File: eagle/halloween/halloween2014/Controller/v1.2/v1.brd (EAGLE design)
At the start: 99.2 x 69.3 mm, 74 parts, among them CON1 SPI, J1 RJ12, J2 RJ12, J3 RJ12, J4 RJ12, J5 RJ12, Q1 BSP75, Q10 BSP75, Q11 BSP75, Q12 BSP75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

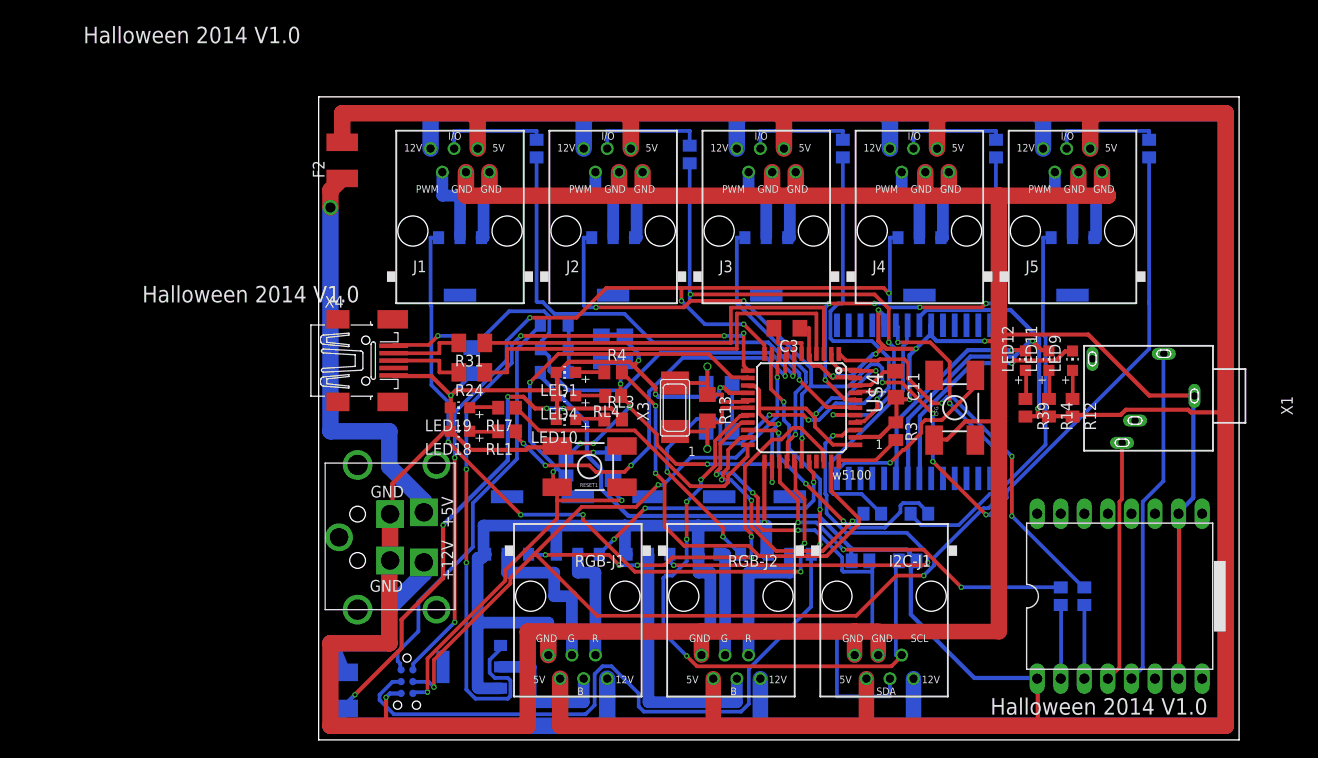
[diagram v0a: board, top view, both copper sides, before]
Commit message: Update halloween, corredt D8 - D10
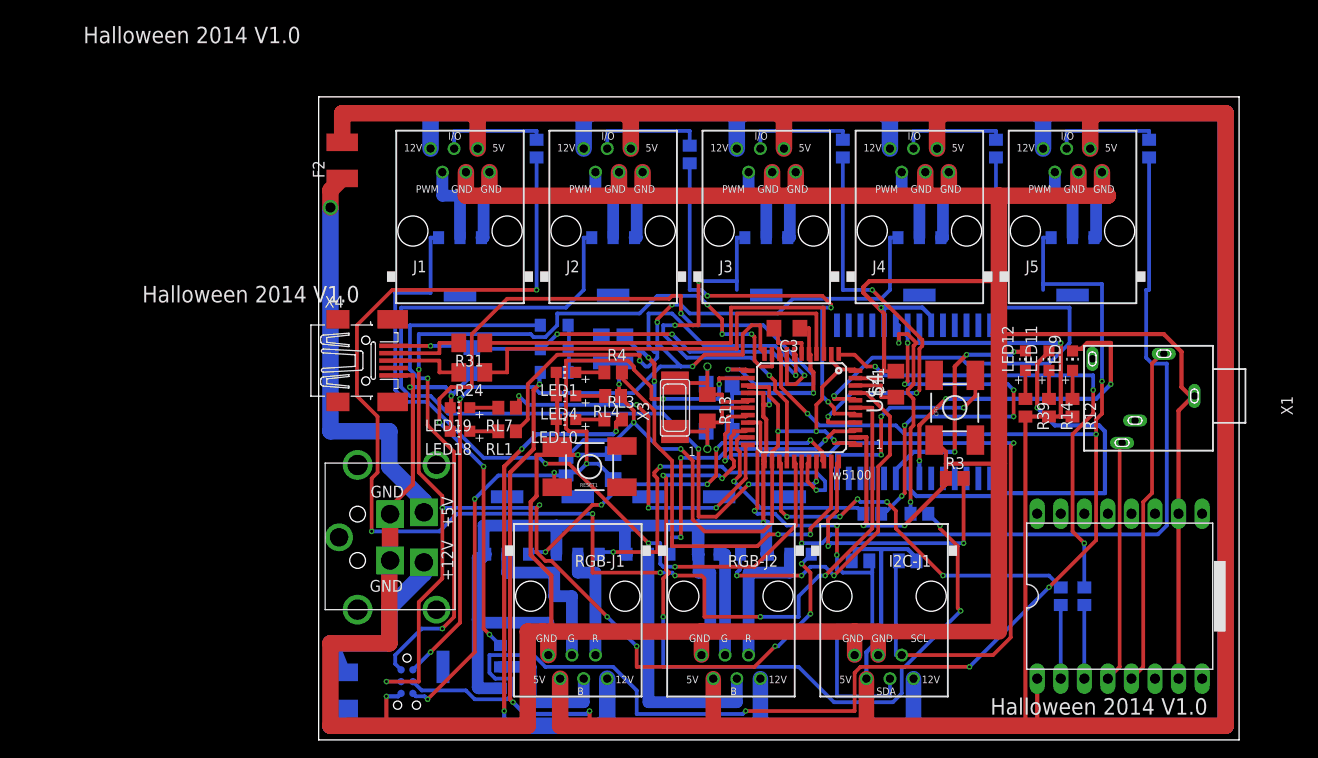
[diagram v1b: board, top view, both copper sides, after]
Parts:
- moved R3 8.13 mm to (68.6, 27.9), turned to 0 degrees
- turned C11 to 90 degrees
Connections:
- net D10*: now also Q2.1
- net D8*: no longer Q2.1
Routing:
- net D10*: track 0.00 -> 94.1 mm, vias 0 -> 3
- net A3: track 55.1 -> 144.2 mm, vias 1 -> 7
- net MOSI: track 94.4 -> 153.8 mm, vias 3 -> 12
- net RX: track 27.4 -> 86.4 mm, vias 3 -> 5
- net GND: track 626.4 -> 661.3 mm, vias 13 -> 12
- net D8*: track 123.1 -> 90.8 mm, vias 7 -> 1
- net SCK: track 150.3 -> 178.4 mm, vias 4 -> 6
- net HWB: track 7.14 -> 31.3 mm, vias 0 -> 2
- net D18*: track 54.0 -> 31.5 mm
- net GND2: track 25.6 -> 44.4 mm
- net SCL: track 67.0 -> 83.7 mm, vias 4 -> 2
- net N$11: track 27.8 -> 44.3 mm, vias 0 -> 6
- net D12*: track 28.9 -> 43.5 mm, vias 1 -> 3
- net ISP+5V: track 43.7 -> 57.9 mm, vias 0 -> 2
- net D11*: track 81.9 -> 95.2 mm
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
